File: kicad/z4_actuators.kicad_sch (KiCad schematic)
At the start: 0 parts

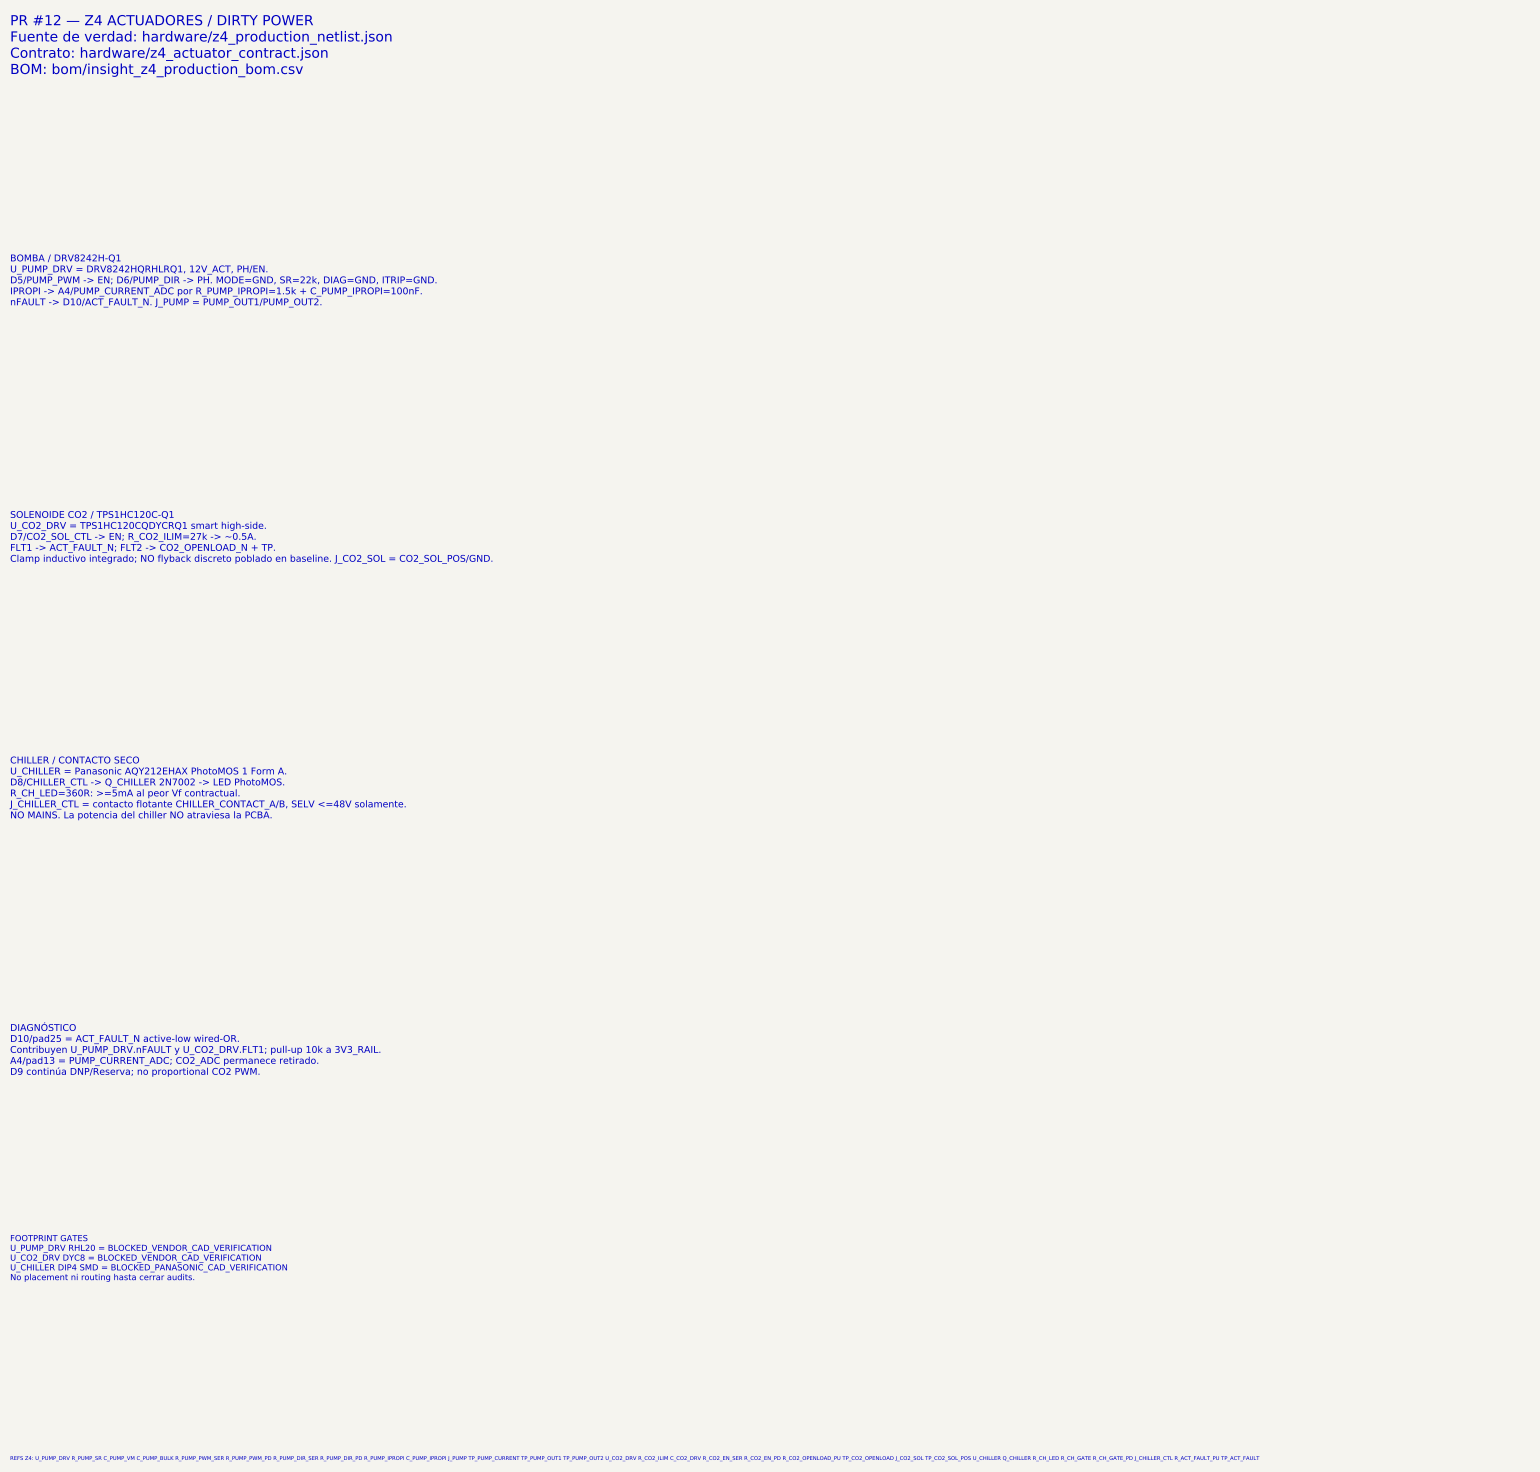
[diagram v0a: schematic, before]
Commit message: eda: actualizar hoja Z4 con footprints cerrados PR13
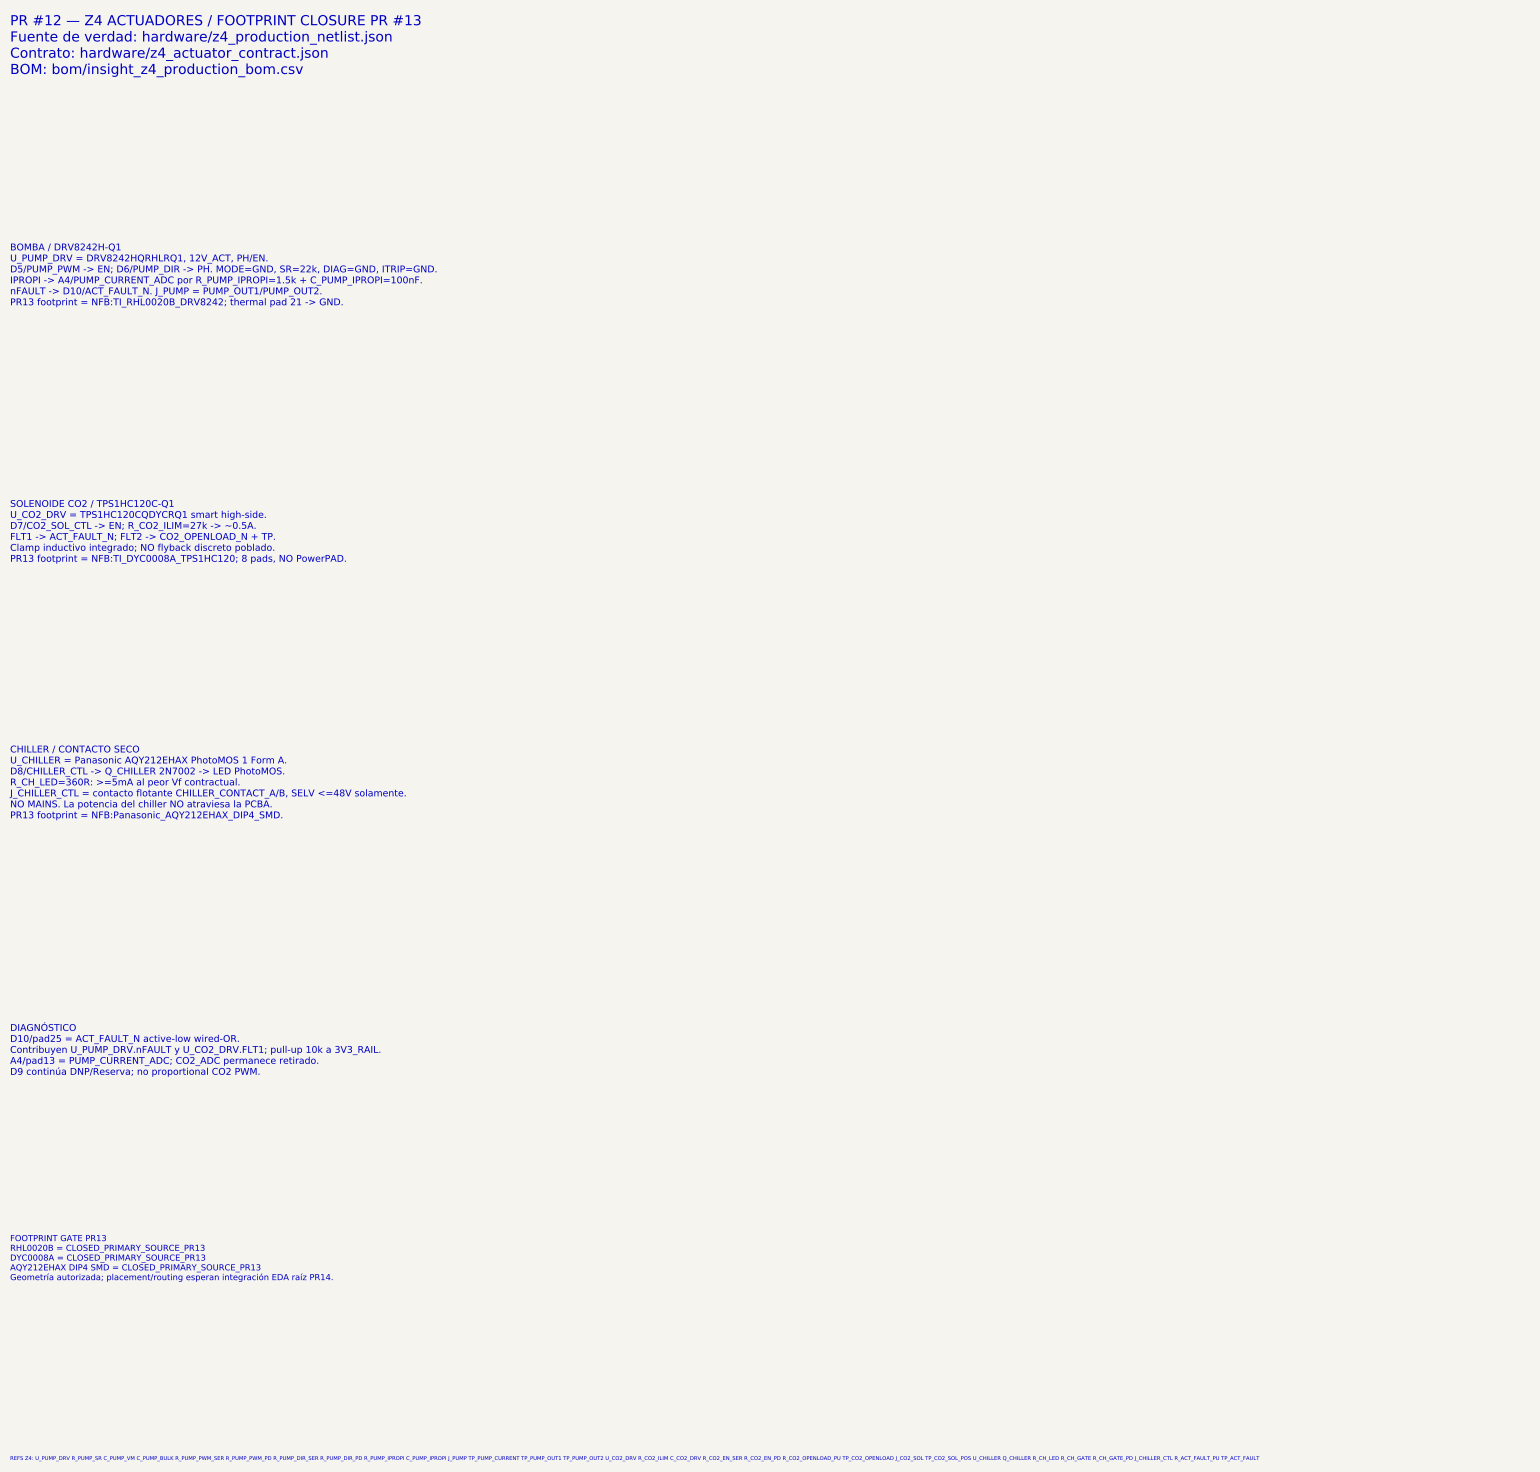
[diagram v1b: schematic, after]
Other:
- note added: "BOMBA / DRV8242H-Q1 U_PUMP_DRV = DRV8242HQRHLRQ1, 12V_ACT, PH/EN. D5/PUMP_PWM -> EN; D6/PUMP_DIR -> PH. MODE=GND, SR=22k, DIAG=GND, ITRIP=GND. IPROPI -> A4/PUMP_CURRENT_ADC por R_PUMP_IPROPI=1.5k + C_PUMP_IPROPI=100nF. nFAULT -> D10/ACT_FAULT_N. J_PUMP = PUMP_OUT1/PUMP_OUT2. PR13 footprint = NFB:TI_RHL0020B_DRV8242; thermal pad 21 -> GND."
- note added: "CHILLER / CONTACTO SECO U_CHILLER = Panasonic AQY212EHAX PhotoMOS 1 Form A. D8/CHILLER_CTL -> Q_CHILLER 2N7002 -> LED PhotoMOS. R_CH_LED=360R: >=5mA al peor Vf contractual. J_CHILLER_CTL = contacto flotante CHILLER_CONTACT_A/B, SELV <=48V solamente. NO MAINS. La potencia del chiller NO atraviesa la PCBA. PR13 footprint = NFB:Panasonic_AQY212EHAX_DIP4_SMD."
- note added: "FOOTPRINT GATE PR13 RHL0020B = CLOSED_PRIMARY_SOURCE_PR13 DYC0008A = CLOSED_PRIMARY_SOURCE_PR13 AQY212EHAX DIP4 SMD = CLOSED_PRIMARY_SOURCE_PR13 Geometría autorizada; placement/routing esperan integración EDA raíz PR14."
- note added: "PR #12 — Z4 ACTUADORES / FOOTPRINT CLOSURE PR #13 Fuente de verdad: hardware/z4_production_netlist.json Contrato: hardware/z4_actuator_contract.json BOM: bom/insight_z4_production_bom.csv"
- note added: "SOLENOIDE CO2 / TPS1HC120C-Q1 U_CO2_DRV = TPS1HC120CQDYCRQ1 smart high-side. D7/CO2_SOL_CTL -> EN; R_CO2_ILIM=27k -> ~0.5A. FLT1 -> ACT_FAULT_N; FLT2 -> CO2_OPENLOAD_N + TP. Clamp inductivo integrado; NO flyback discreto poblado. PR13 footprint = NFB:TI_DYC0008A_TPS1HC120; 8 pads, NO PowerPAD."
- note removed: "BOMBA / DRV8242H-Q1 U_PUMP_DRV = DRV8242HQRHLRQ1, 12V_ACT, PH/EN. D5/PUMP_PWM -> EN; D6/PUMP_DIR -> PH. MODE=GND, SR=22k, DIAG=GND, ITRIP=GND. IPROPI -> A4/PUMP_CURRENT_ADC por R_PUMP_IPROPI=1.5k + C_PUMP_IPROPI=100nF. nFAULT -> D10/ACT_FAULT_N. J_PUMP = PUMP_OUT1/PUMP_OUT2."
- note removed: "CHILLER / CONTACTO SECO U_CHILLER = Panasonic AQY212EHAX PhotoMOS 1 Form A. D8/CHILLER_CTL -> Q_CHILLER 2N7002 -> LED PhotoMOS. R_CH_LED=360R: >=5mA al peor Vf contractual. J_CHILLER_CTL = contacto flotante CHILLER_CONTACT_A/B, SELV <=48V solamente. NO MAINS. La potencia del chiller NO atraviesa la PCBA."
- note removed: "FOOTPRINT GATES U_PUMP_DRV RHL20 = BLOCKED_VENDOR_CAD_VERIFICATION U_CO2_DRV DYC8 = BLOCKED_VENDOR_CAD_VERIFICATION U_CHILLER DIP4 SMD = BLOCKED_PANASONIC_CAD_VERIFICATION No placement ni routing hasta cerrar audits."
- note removed: "PR #12 — Z4 ACTUADORES / DIRTY POWER Fuente de verdad: hardware/z4_production_netlist.json Contrato: hardware/z4_actuator_contract.json BOM: bom/insight_z4_production_bom.csv"
- note removed: "SOLENOIDE CO2 / TPS1HC120C-Q1 U_CO2_DRV = TPS1HC120CQDYCRQ1 smart high-side. D7/CO2_SOL_CTL -> EN; R_CO2_ILIM=27k -> ~0.5A. FLT1 -> ACT_FAULT_N; FLT2 -> CO2_OPENLOAD_N + TP. Clamp inductivo integrado; NO flyback discreto poblado en baseline. J_CO2_SOL = CO2_SOL_POS/GND."
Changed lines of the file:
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@@
   (version 20250114)
   (generator "nfb_pr12_z4_contract")
-  (generator_version "1.0")
+  (generator_version "1.1")
   (paper "A3")
   (title_block
     (title "NFB Insight PCBA v2 — Z4 Actuadores / Dirty Power")
     (date "2026-08-12")
-    (rev "0.12.0")
+    (rev "0.13.0")
     (company "Cafelium SRL / Nebula Ecosystem")
-    (comment 1 "PR #12 — contrato Z4 gobernado por hardware/z4_production_netlist.json")
+    (comment 1 "PR #12 electrical baseline; footprints físicos cerrados por PR #13")
     (comment 2 "DRV8242H-Q1 | TPS1HC120C-Q1 | AQY212EHAX")
-    (comment 3 "Placement/routing fuera de alcance; footprints críticos bloqueados")
+    (comment 3 "Placement/routing todavía fuera de alcance")
     (comment 4 "Chiller = contacto seco aislado SELV <=48V; NO MAINS")
   )
-  (text "PR #12 — Z4 ACTUADORES / DIRTY POWER\nFuente de verdad: hardware/z4_production_netlist.json\nContrato: hardware/z4_actuator_contract.json\nBOM: bom/insight_z4_production_bom.csv"
+  (text "PR #12 — Z4 ACTUADORES / FOOTPRINT CLOSURE PR #13\nFuente de verdad: hardware/z4_production_netlist.json\nContrato: hardware/z4_actuator_contract.json\nBOM: bom/insight_z4_production_bom.csv"
     (exclude_from_sim no)
     (at 30.48 30.48 0)
     (effects (font (size 2 2)) (justify left bottom))
   )
-  (text "BOMBA / DRV8242H-Q1\nU_PUMP_DRV = DRV8242HQRHLRQ1, 12V_ACT, PH/EN.\nD5/PUMP_PWM -> EN; D6/PUMP_DIR -> PH. MODE=GND, SR=22k, DIAG=GND, ITRIP=GND.\nIPROPI -> A4/PUMP_CURRENT_ADC por R_PUMP_IPROPI=1.5k + C_PUMP_IPROPI=100nF.\nnFAULT -> D10/ACT_FAULT_N. J_PUMP = PUMP_OUT1/PUMP_OUT2."
+  (text "BOMBA / DRV8242H-Q1\nU_PUMP_DRV = DRV8242HQRHLRQ1, 12V_ACT, PH/EN.\nD5/PUMP_PWM -> EN; D6/PUMP_DIR -> PH. MODE=GND, SR=22k, DIAG=GND, ITRIP=GND.\nIPROPI -> A4/PUMP_CURRENT_ADC por R_PUMP_IPROPI=1.5k + C_PUMP_IPROPI=100nF.\nnFAULT -> D10/ACT_FAULT_N. J_PUMP = PUMP_OUT1/PUMP_OUT2.\nPR13 footprint = NFB:TI_RHL0020B_DRV8242; thermal pad 21 -> GND."
     (exclude_from_sim no)
     (at 30.48 76.2 0)
     (effects (font (size 1.35 1.35)) (justify left bottom))
   )
-  (text "SOLENOIDE CO2 / TPS1HC120C-Q1\nU_CO2_DRV = TPS1HC120CQDYCRQ1 smart high-side.\nD7/CO2_SOL_CTL -> EN; R_CO2_ILIM=27k -> ~0.5A.\nFLT1 -> ACT_FAULT_N; FLT2 -> CO2_OPENLOAD_N + TP.\nClamp inductivo integrado; NO flyback discreto poblado en baseline. J_CO2_SOL = CO2_SOL_POS/GND."
+  (text "SOLENOIDE CO2 / TPS1HC120C-Q1\nU_CO2_DRV = TPS1HC120CQDYCRQ1 smart high-side.\nD7/CO2_SOL_CTL -> EN; R_CO2_ILIM=27k -> ~0.5A.\nFLT1 -> ACT_FAULT_N; FLT2 -> CO2_OPENLOAD_N + TP.\nClamp inductivo integrado; NO flyback discreto poblado.\nPR13 footprint = NFB:TI_DYC0008A_TPS1HC120; 8 pads, NO PowerPAD."
     (exclude_from_sim no)
     (at 30.48 127 0)
     (effects (font (size 1.35 1.35)) (justify left bottom))
   )
-  (text "CHILLER / CONTACTO SECO\nU_CHILLER = Panasonic AQY212EHAX PhotoMOS 1 Form A.\nD8/CHILLER_CTL -> Q_CHILLER 2N7002 -> LED PhotoMOS.\nR_CH_LED=360R: >=5mA al peor Vf contractual.\nJ_CHILLER_CTL = contacto flotante CHILLER_CONTACT_A/B, SELV <=48V solamente.\nNO MAINS. La potencia del chiller NO atraviesa la PCBA."
+  (text "CHILLER / CONTACTO SECO\nU_CHILLER = Panasonic AQY212EHAX PhotoMOS 1 Form A.\nD8/CHILLER_CTL -> Q_CHILLER 2N7002 -> LED PhotoMOS.\nR_CH_LED=360R: >=5mA al peor Vf contractual.\nJ_CHILLER_CTL = contacto flotante CHILLER_CONTACT_A/B, SELV <=48V solamente.\nNO MAINS. La potencia del chiller NO atraviesa la PCBA.\nPR13 footprint = NFB:Panasonic_AQY212EHAX_DIP4_SMD."
     (exclude_from_sim no)
     (at 30.48 177.8 0)
@@
     (effects (font (size 1.35 1.35)) (justify left bottom))
   )
-  (text "FOOTPRINT GATES\nU_PUMP_DRV RHL20 = BLOCKED_VENDOR_CAD_VERIFICATION\nU_CO2_DRV DYC8 = BLOCKED_VENDOR_CAD_VERIFICATION\nU_CHILLER DIP4 SMD = BLOCKED_PANASONIC_CAD_VERIFICATION\nNo placement ni routing hasta cerrar audits."
+  (text "FOOTPRINT GATE PR13\nRHL0020B = CLOSED_PRIMARY_SOURCE_PR13\nDYC0008A = CLOSED_PRIMARY_SOURCE_PR13\nAQY212EHAX DIP4 SMD = CLOSED_PRIMARY_SOURCE_PR13\nGeometría autorizada; placement/routing esperan integración EDA raíz PR14."
     (exclude_from_sim no)
     (at 30.48 269.24 0)
